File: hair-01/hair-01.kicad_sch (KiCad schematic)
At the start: 9 parts, among them J1 TYPE-C-31-M-12, U1 ESP-12F

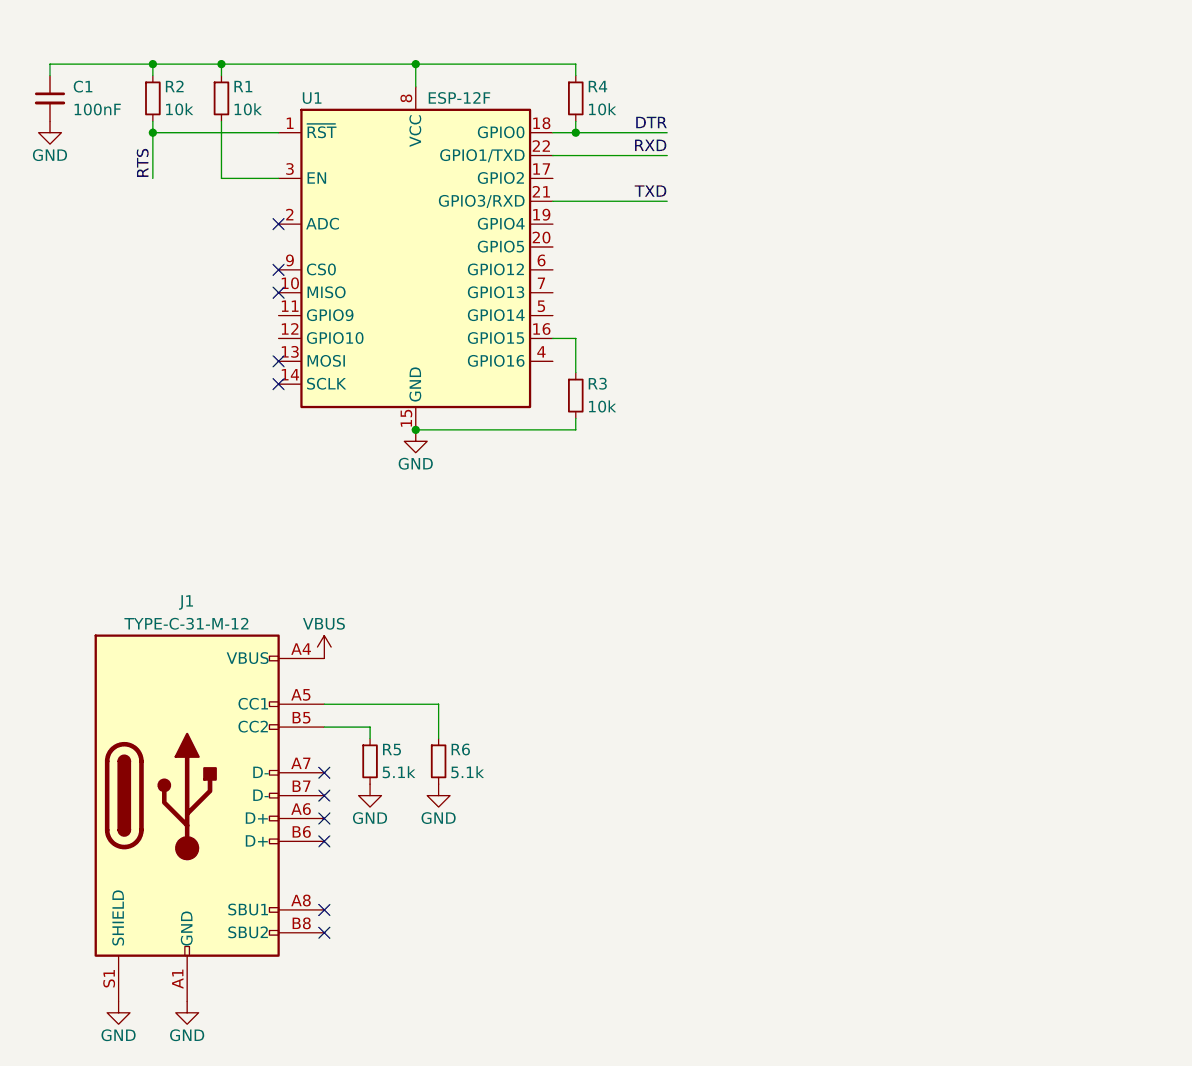
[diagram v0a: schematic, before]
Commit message: hair-01: Add AP2112
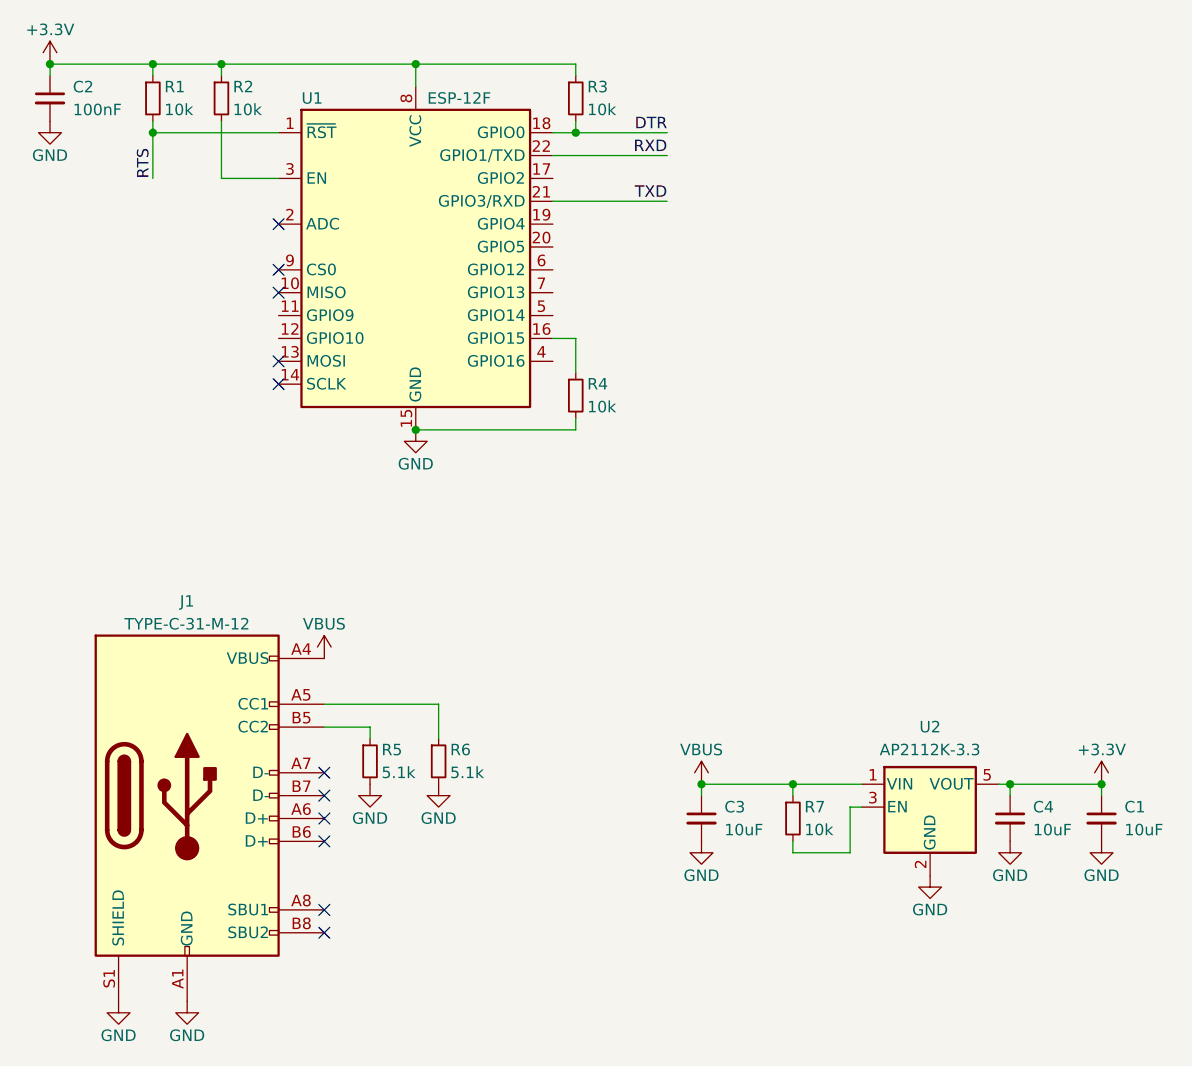
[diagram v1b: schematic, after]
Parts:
- added C1, C3, C4: 10uF, Capacitor_SMD:C_1206_3216Metric, symbol Device:C_Small
- added R7: 10k, Resistor_SMD:R_0805_2012Metric, symbol Device:R_Small
- added U2: AP2112K-3.3, Package_TO_SOT_SMD:SOT-23-5, symbol Regulator_Linear:AP2112K-3.3
- C2: renamed from C1; footprint Capacitor_SMD:C_0603_1608Metric -> Capacitor_SMD:C_0805_2012Metric; LCSC C14663 -> C519981
- R1: renamed from R2; footprint Resistor_SMD:R_0603_1608Metric -> Resistor_SMD:R_0805_2012Metric; LCSC C98220 -> C84376
- R2: renamed from R1; footprint Resistor_SMD:R_0603_1608Metric -> Resistor_SMD:R_0805_2012Metric; LCSC C98220 -> C84376
- R3: renamed from R4; footprint Resistor_SMD:R_0603_1608Metric -> Resistor_SMD:R_0805_2012Metric; LCSC C98220 -> C84376
- R4: renamed from R3; footprint Resistor_SMD:R_0603_1608Metric -> Resistor_SMD:R_0805_2012Metric; LCSC C98220 -> C84376
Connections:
- net GND: now also C1.2, C3.2, C4.2, U2.2 (GND)
- net VBUS: now also C3.1, R7.1, U2.1 (VIN)
- net +3V3: now reaches C2.1, R1.1, R2.1, R3.1, U1.8 (VCC)
- net +3V3: now also C1.1, C4.1, U2.5 (VOUT)
- new net: R7.2, U2.3 (EN)

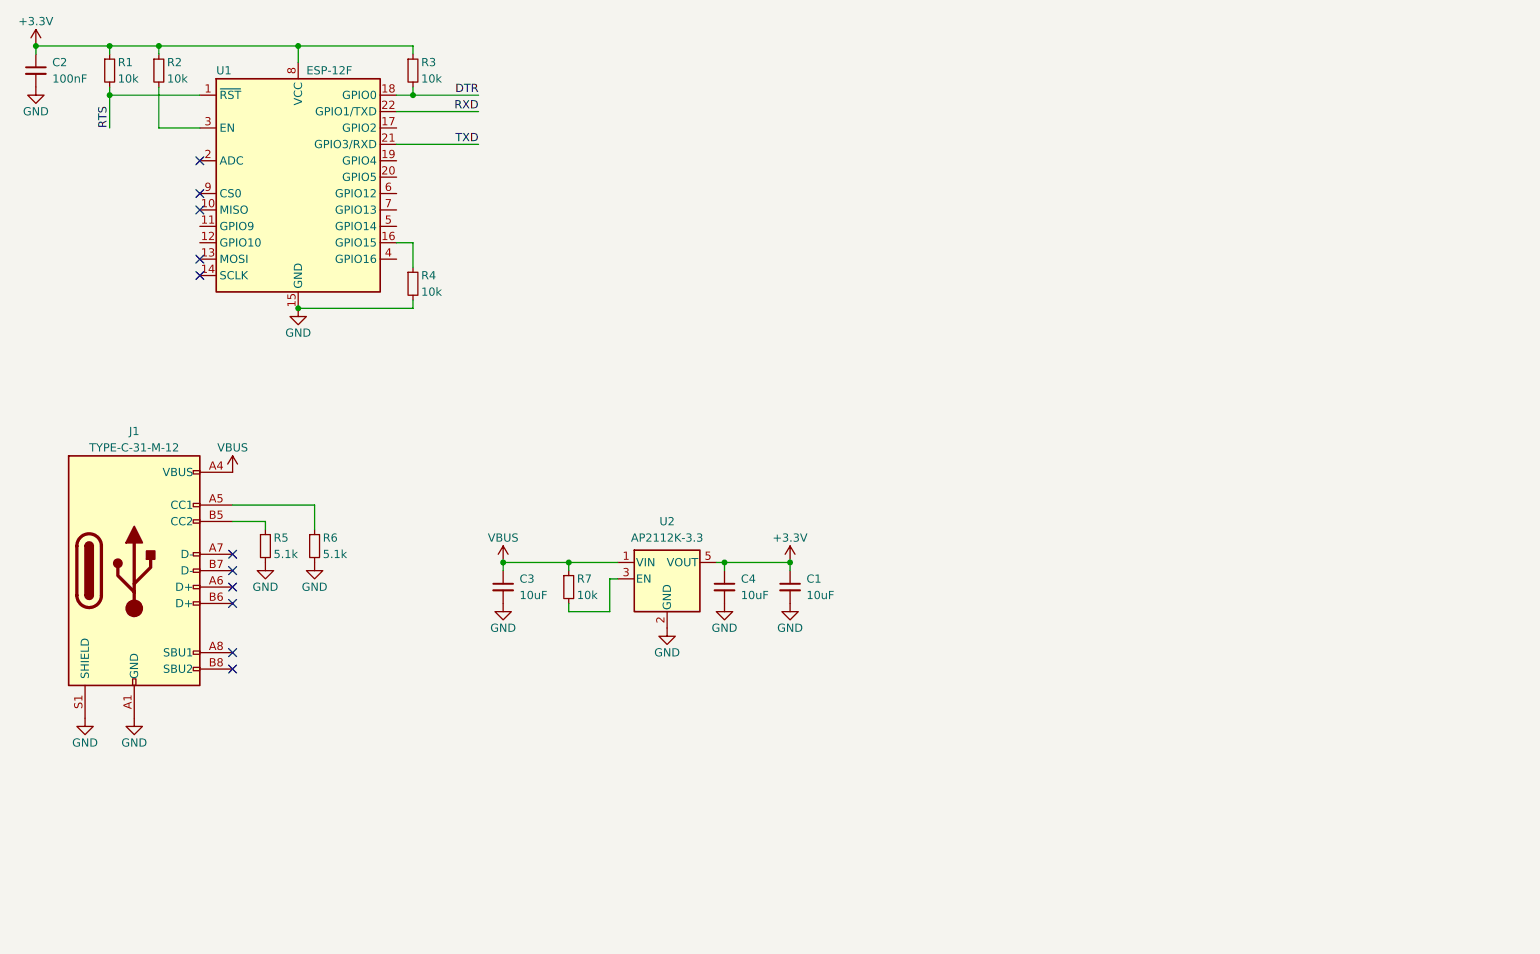
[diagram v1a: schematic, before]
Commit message: hair-01: Add reset button and auto-reset
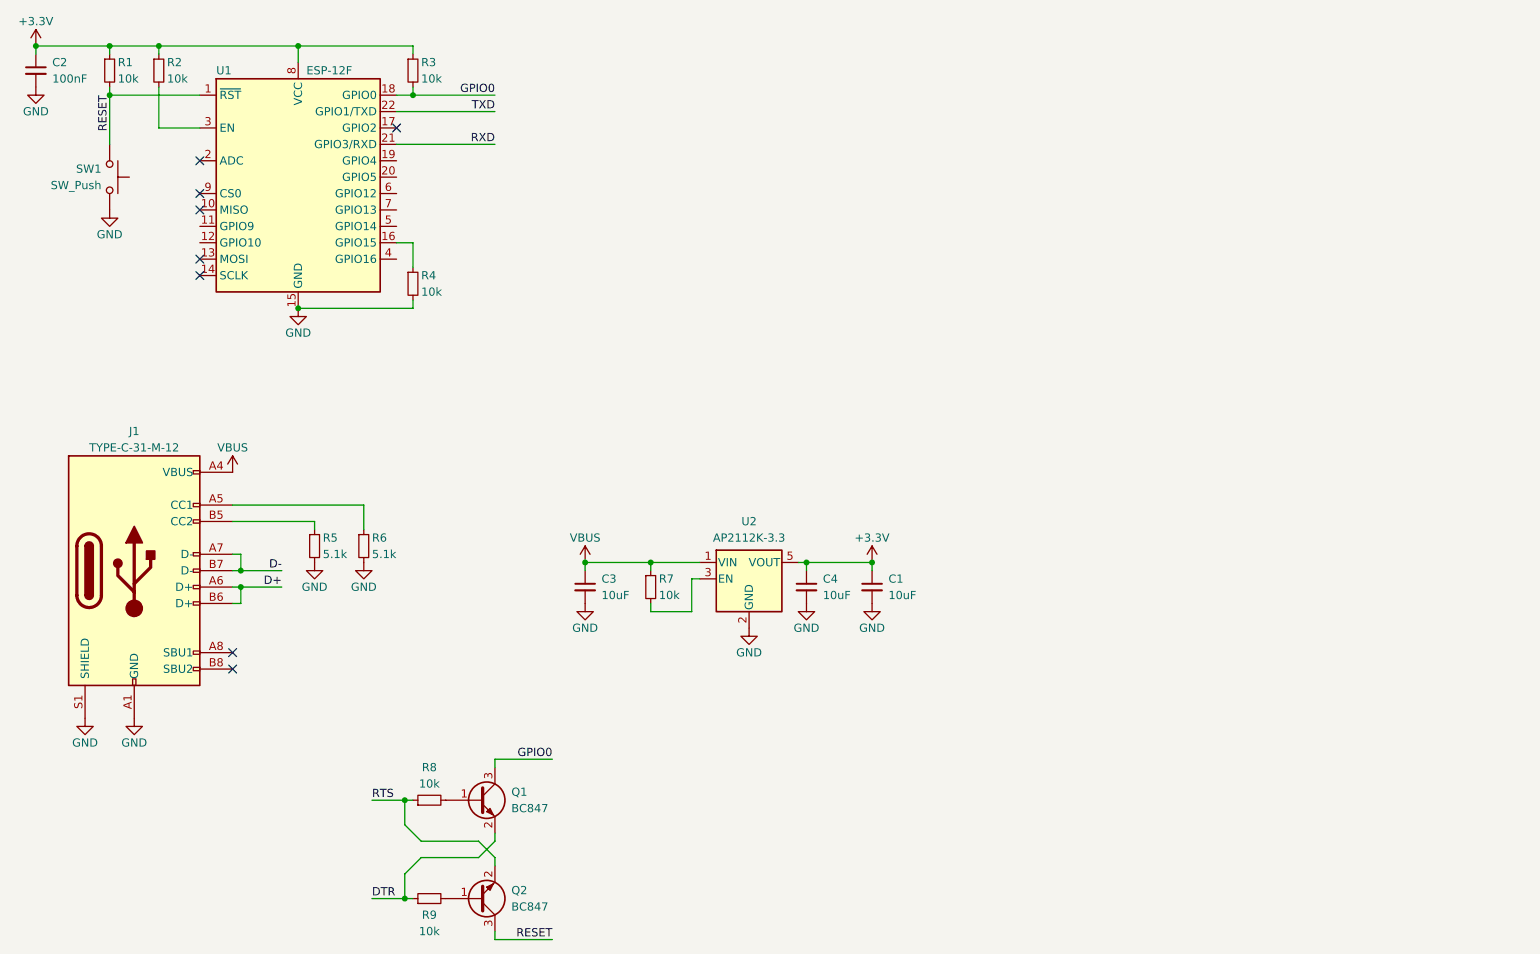
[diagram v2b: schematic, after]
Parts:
- added Q1, Q2: BC847, Package_TO_SOT_SMD:SOT-23, symbol Transistor_BJT:BC847
- added R8, R9: 10k, Resistor_SMD:R_0805_2012Metric, symbol Device:R_Small
- added SW1: SW_Push, Button_Switch_SMD:SW_Push_1P1T-MP_NO_Horizontal_Alps_SKRTLAE010, symbol Switch:SW_Push
- C1, C3, C4: LCSC C109464 -> C13585
- C2: LCSC C519981 -> C49678
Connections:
- net DTR: now also Q1.2 (E), R9.1; no longer R3.2, U1.18 (GPIO0)
- net GND: now also SW1.2
- net RTS: now also Q2.2 (E), R8.1; no longer R1.2, U1.1 (~{RST})
- net RXD: now also U1.21 (GPIO3/RXD); no longer U1.22 (GPIO1/TXD)
- net TXD: now also U1.22 (GPIO1/TXD); no longer U1.21 (GPIO3/RXD)
- net D+: now reaches J1.A6 (D+)
- net D+: now also J1.B6 (D+)
- net D-: now reaches J1.A7 (D-)
- net D-: now also J1.B7 (D-)
- new net: Q1.1 (B), R8.2
- new net: Q2.1 (B), R9.2
- new net GPIO0: Q1.3 (C), R3.2, U1.18 (GPIO0)
- new net RESET: Q2.3 (C), R1.2, SW1.1, U1.1 (~{RST})
- no-connect marks 11 -> 8
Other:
- moved on the sheet: C1, C3, C4, R5, R6, R7, U2

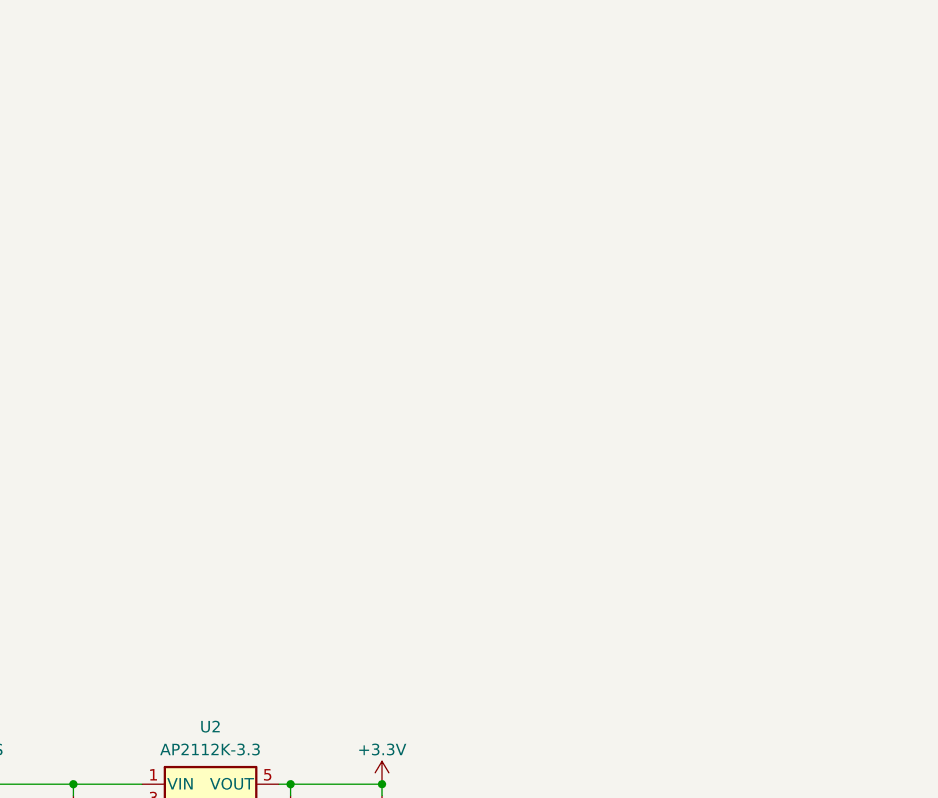
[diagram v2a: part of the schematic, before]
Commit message: hair-01: Add CP2102N
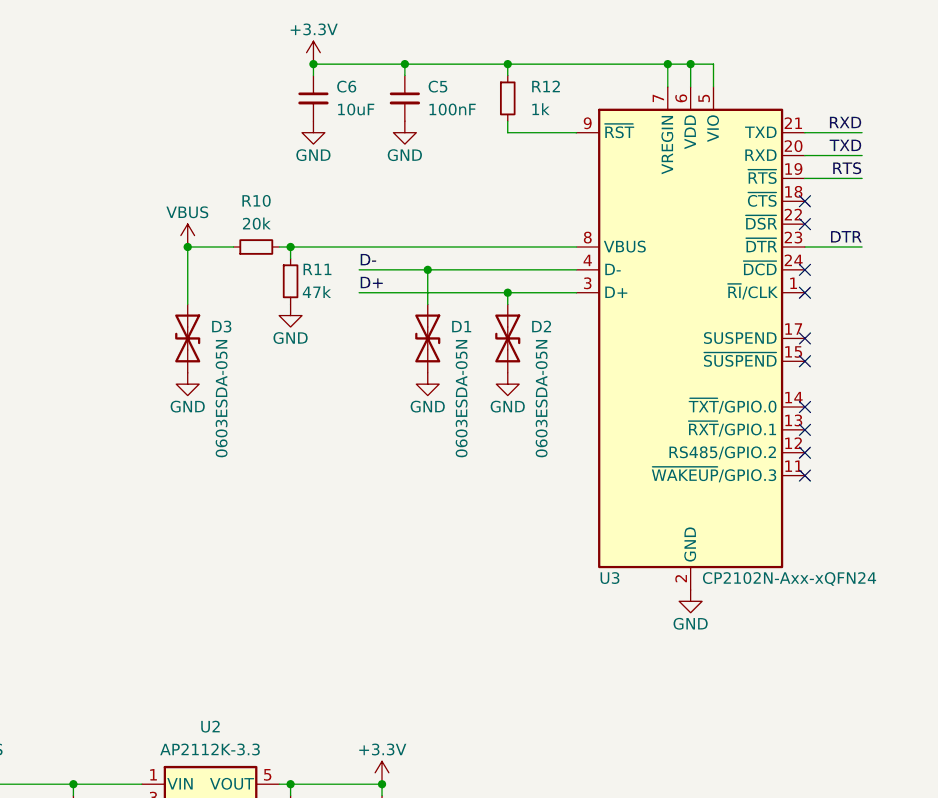
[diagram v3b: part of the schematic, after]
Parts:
- added C5: 100nF, Capacitor_SMD:C_0805_2012Metric, symbol Device:C_Small
- added C6: 10uF, Capacitor_SMD:C_1206_3216Metric, symbol Device:C_Small
- added D1, D2, D3: 0603ESDA-05N, Diode_SMD:D_0603_1608Metric, symbol Device:D_TVS
- added R10: 20k, Resistor_SMD:R_0603_1608Metric, symbol Device:R_Small
- added R11: 47k, Resistor_SMD:R_0603_1608Metric, symbol Device:R_Small
- added R12: 1k, Resistor_SMD:R_0603_1608Metric, symbol Device:R_Small
- added U3: CP2102N-Axx-xQFN24, Package_DFN_QFN:SiliconLabs_QFN-20-1EP_3x3mm_P0.5mm, symbol Interface_USB:CP2102N-Axx-xQFN24
- R1, R2, R3, R4, R7, R8, R9: LCSC C84376 -> C17414
- R5, R6: LCSC C105580 -> C23186
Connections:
- net +3V3: now also C5.1, C6.1, R12.1, U3.5 (VIO), U3.6 (VDD), U3.7 (VREGIN)
- net D+: now also D2.1 (A1), U3.3 (D+)
- net D-: now also D1.1 (A1), U3.4 (D-)
- net DTR: now also U3.23 (~{DTR})
- net GND: now also C5.2, C6.2, D1.2 (A2), D2.2 (A2), D3.2 (A2), R11.2, U3.2 (GND), U3.25 (GND)
- net RTS: now also U3.19 (~{RTS})
- net RXD: now also U3.21 (TXD)
- net TXD: now also U3.20 (RXD)
- net VBUS: now also D3.1 (A1), R10.1
- new net: R10.2, R11.1, U3.8 (VBUS)
- new net: R12.2, U3.9 (~{RST})
- no-connect marks 8 -> 18
